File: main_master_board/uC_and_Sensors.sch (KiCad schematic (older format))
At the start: 41 parts, among them P14 CONN_01X05, U1 NRF24L01+, U15 DSPIC33EP512GP806-I/PT, U16 DWM1000, U29 RGB_LED, U30 RGB_LED, U31 Si1900DL, U32 Si1900DL, U9 Si1900DL

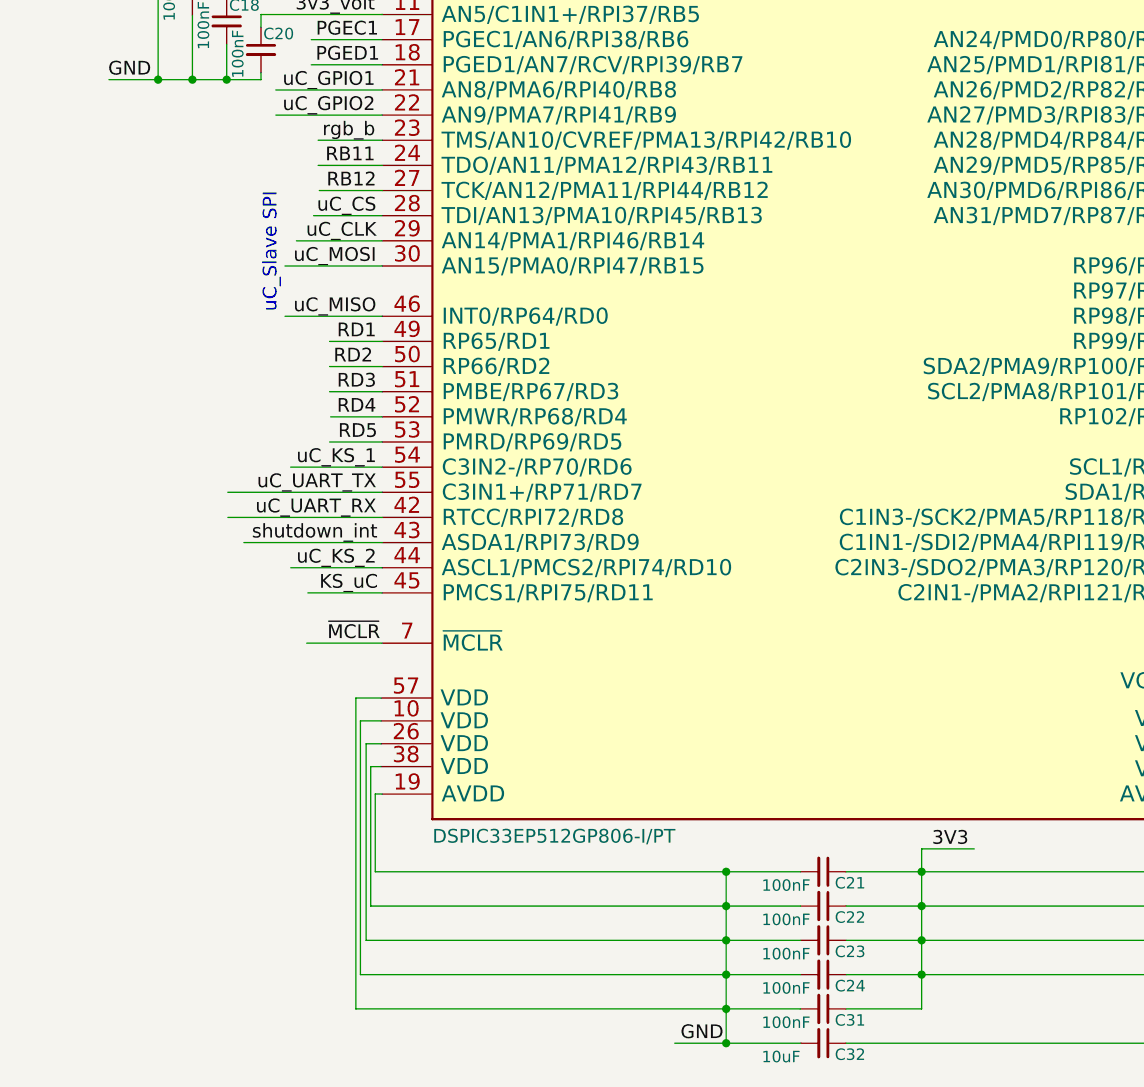
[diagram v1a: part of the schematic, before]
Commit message: more routing. Started on PIC now.
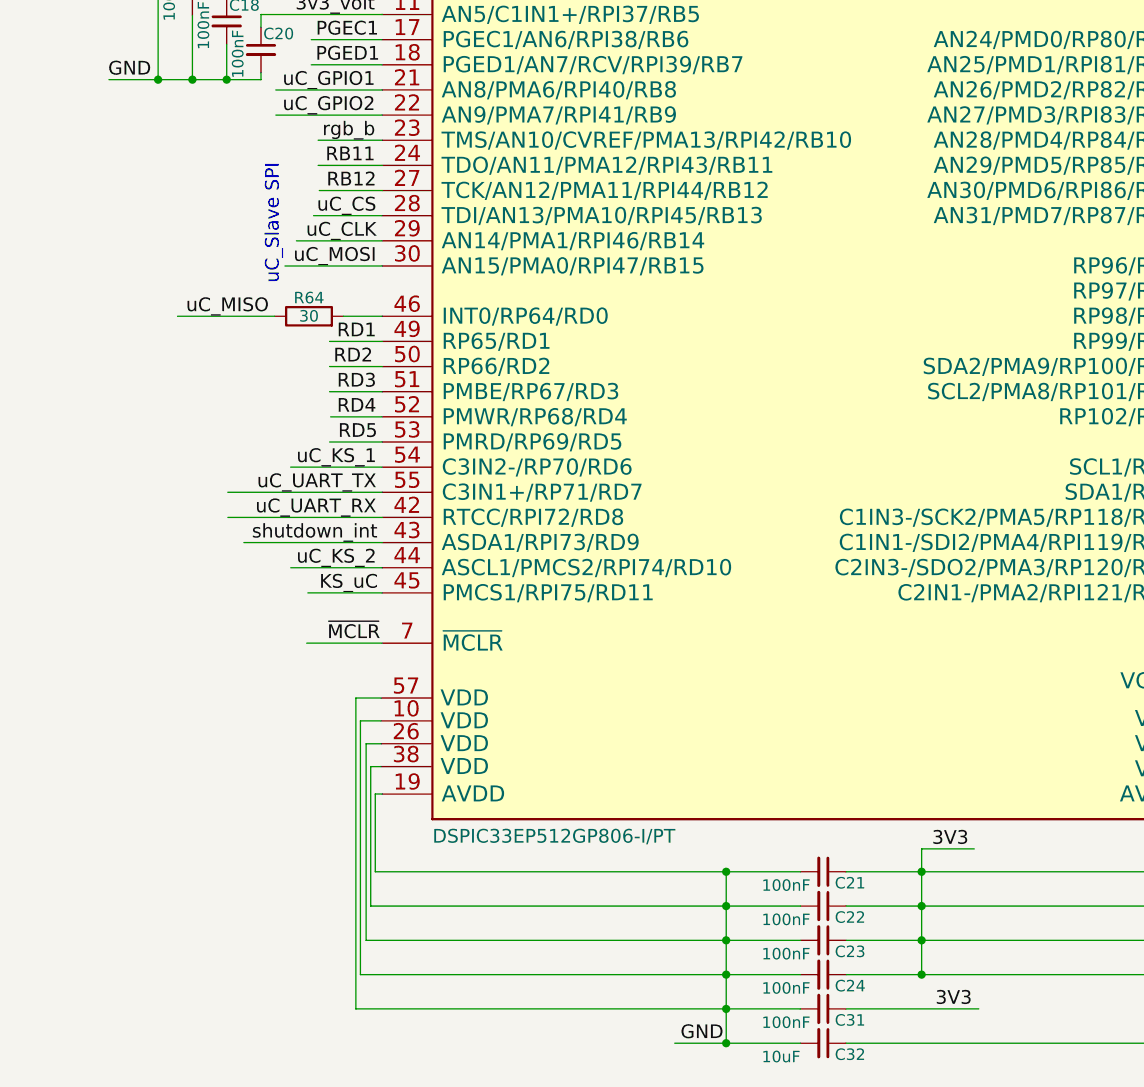
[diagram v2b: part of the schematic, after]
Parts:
- added R64: 30, Resistors_SMD:R_0402, symbol R
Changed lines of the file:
@@
 LIBS:Sensors
 LIBS:LP3852-3.3
-LIBS:decaWave
+LIBS:0s102011ma1qn1
+LIBS:74LVC1G17
+LIBS:74V1T126
+LIBS:acs711klctr-12ab-t
+LIBS:AD7192
+LIBS:AD7193
+LIBS:am-hrr30-xxx
+LIBS:aon7528
+LIBS:AP7363
+LIBS:AS1359
+LIBS:csd16323q3
+LIBS:dmn2004dmk
+LIBS:dp_devices
+LIBS:DSPIC33E128MC506
+LIBS:fds6898az
+LIBS:ina197
+LIBS:irf7329pbf
+LIBS:ld1117
+LIBS:lm3478
+LIBS:lm3481
+LIBS:lt1910
+LIBS:ltc1871
+LIBS:ltc1982
+LIBS:MAG3110
+LIBS:mcp1700
+LIBS:mcp73831
+LIBS:mcsmt-g5030a1-3712
+LIBS:microchip_can
+LIBS:microclasp_hdrx2
+LIBS:microclasp_hdrx3
+LIBS:MPU-6000_MPU-6050
+LIBS:MPU-9150
+LIBS:nrf24l01+
+LIBS:pds1040l
+LIBS:pic12f1571
+LIBS:pinhead
+LIBS:psmn013-80ys
+LIBS:RESISTOR_ARRAY
+LIBS:rf803d
+LIBS:RGB_LED
+LIBS:Si1970DH
+LIBS:sn65hvd232
+LIBS:ssc54
+LIBS:sw_push_4
+LIBS:tc74
+LIBS:TPS2113A
+LIBS:tps54540
+LIBS:vs-mbrb1635pbf
+LIBS:xal5050-562meb
+LIBS:xal6030-182mec
 LIBS:conn_2x50
 LIBS:conn_open_q_x2
@@
 LIBS:ac-dc
 LIBS:actel
-LIBS:allegro
 LIBS:Altera
 LIBS:analog_devices
@@
 LIBS:logo
 LIBS:maxim
-LIBS:mechanical
 LIBS:microchip_dspic33dsc
 LIBS:microchip_pic10mcu
@@
 LIBS:microchip_pic32mcu
 LIBS:motor_drivers
-LIBS:motors
 LIBS:msp430
 LIBS:nordicsemi
@@
 LIBS:ttl_ieee
 LIBS:video
-LIBS:wiznet
 LIBS:Worldsemi
 LIBS:Xicor
-LIBS:zetex
 LIBS:Zilog
 LIBS:conn_2x45
@@
 Text Label 9105 5345 2    60   ~ 0
 uC_MOSI
-Text Label 9105 5565 2    60   ~ 0
+Text Label 8635 5565 2    60   ~ 0
 uC_MISO
 Text Label 9105 5125 2    60   ~ 0
@@
 Text Notes 1025 2650 0    60   ~ 0
 uC_Slave SPI
-Text Notes 8675 5025 3    60   ~ 0
+Text Notes 8685 4900 3    60   ~ 0
 uC_Slave SPI
 Text Label 12895 3695 0    60   ~ 0
@@
 	9015 8595 10960 8595
 Wire Wire Line
-	11160 8595 11490 8595
-Wire Wire Line
-	11490 8595 11490 8445
-Connection ~ 11490 8445
-Wire Wire Line
-	11490 7895 11490 8440
-Connection ~ 11490 8295
-Connection ~ 11490 8145
-Connection ~ 11490 7995
+	11160 8595 11740 8595
 Wire Wire Line
 	11490 7895 11720 7895
@@
 	9130 5345 8705 5345
 Wire Wire Line
-	9130 5565 8705 5565
+	8660 5565 8235 5565
 Wire Wire Line
 	9130 5125 8830 5125
@@
 Wire Wire Line
 	9975 2625 10025 2625
+Text Label 11550 8595 0    60   ~ 0
+3V3
+Connection ~ 11490 8445
+Wire Wire Line
+	11490 7895 11490 8445
+Connection ~ 11490 8295
+Connection ~ 11490 8145
+Connection ~ 11490 7995
+$Comp
+L R R64
+U 1 1 58A3588B
+P 8810 5565
+F 0 "R64" V 8890 5565 50  0000 C CNN
+F 1 "30" V 8810 5565 50  0000 C CNN
+F 2 "Resistors_SMD:R_0402" V 8740 5565 50  0001 C CNN
+F 3 "" H 8810 5565 50  0000 C CNN
+	1    8810 5565
+	0    -1   -1   0
+$EndComp
+Wire Wire Line
+	8960 5565 9130 5565
 $EndSCHEMATC

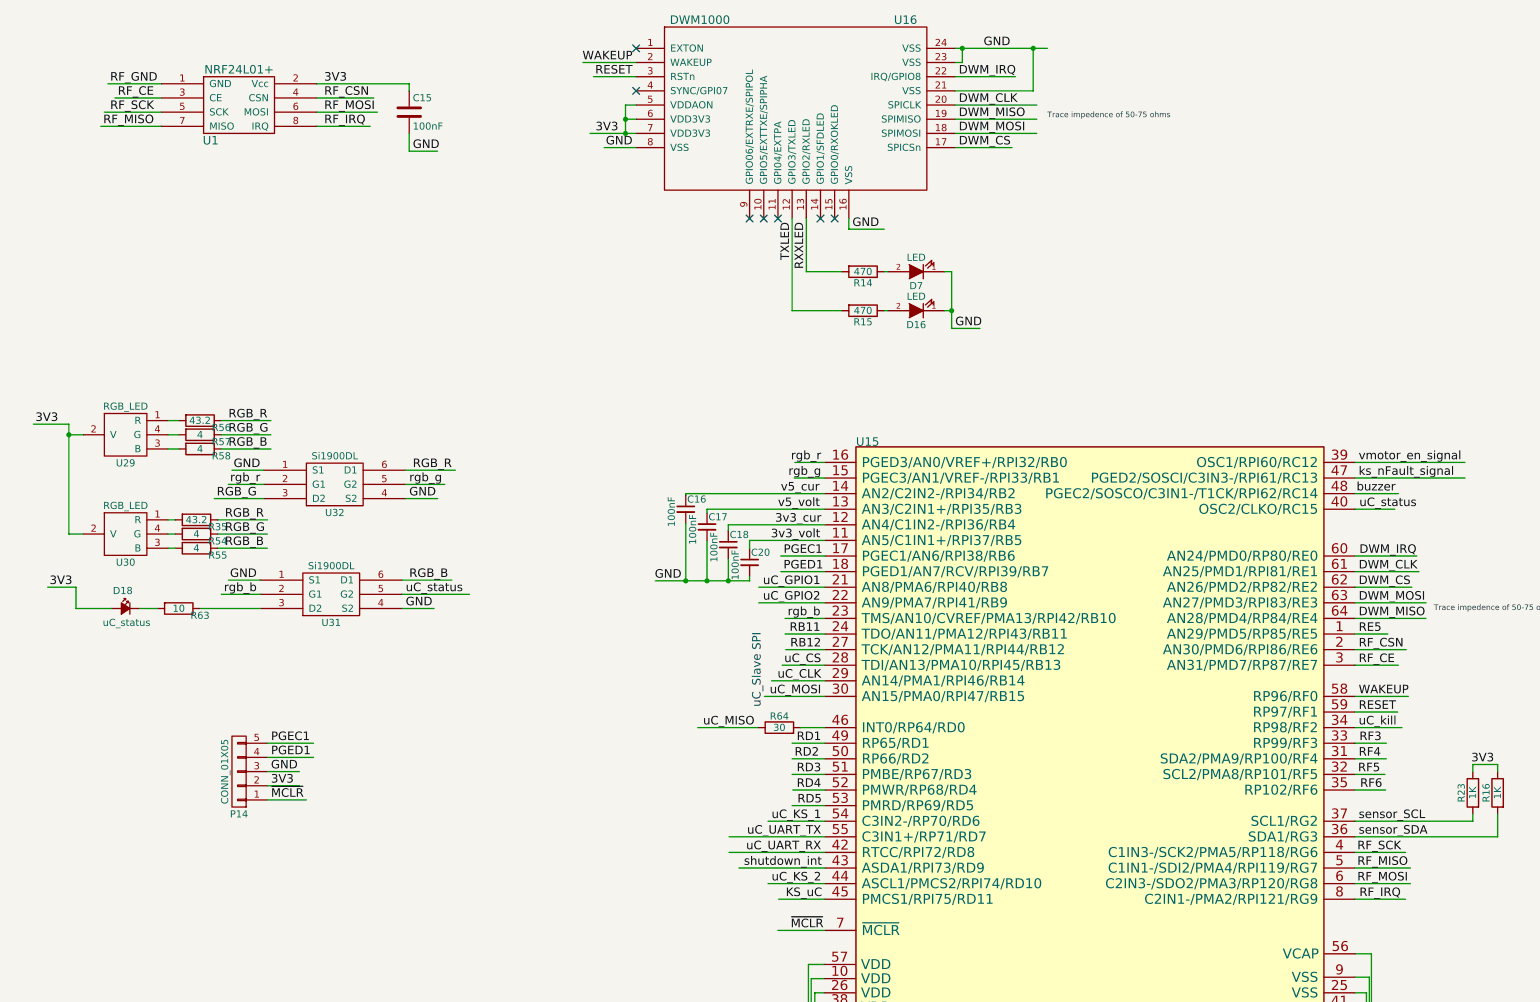
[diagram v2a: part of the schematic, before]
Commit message: Routing the RGB leds. Also finished the dwm and nrf24L01
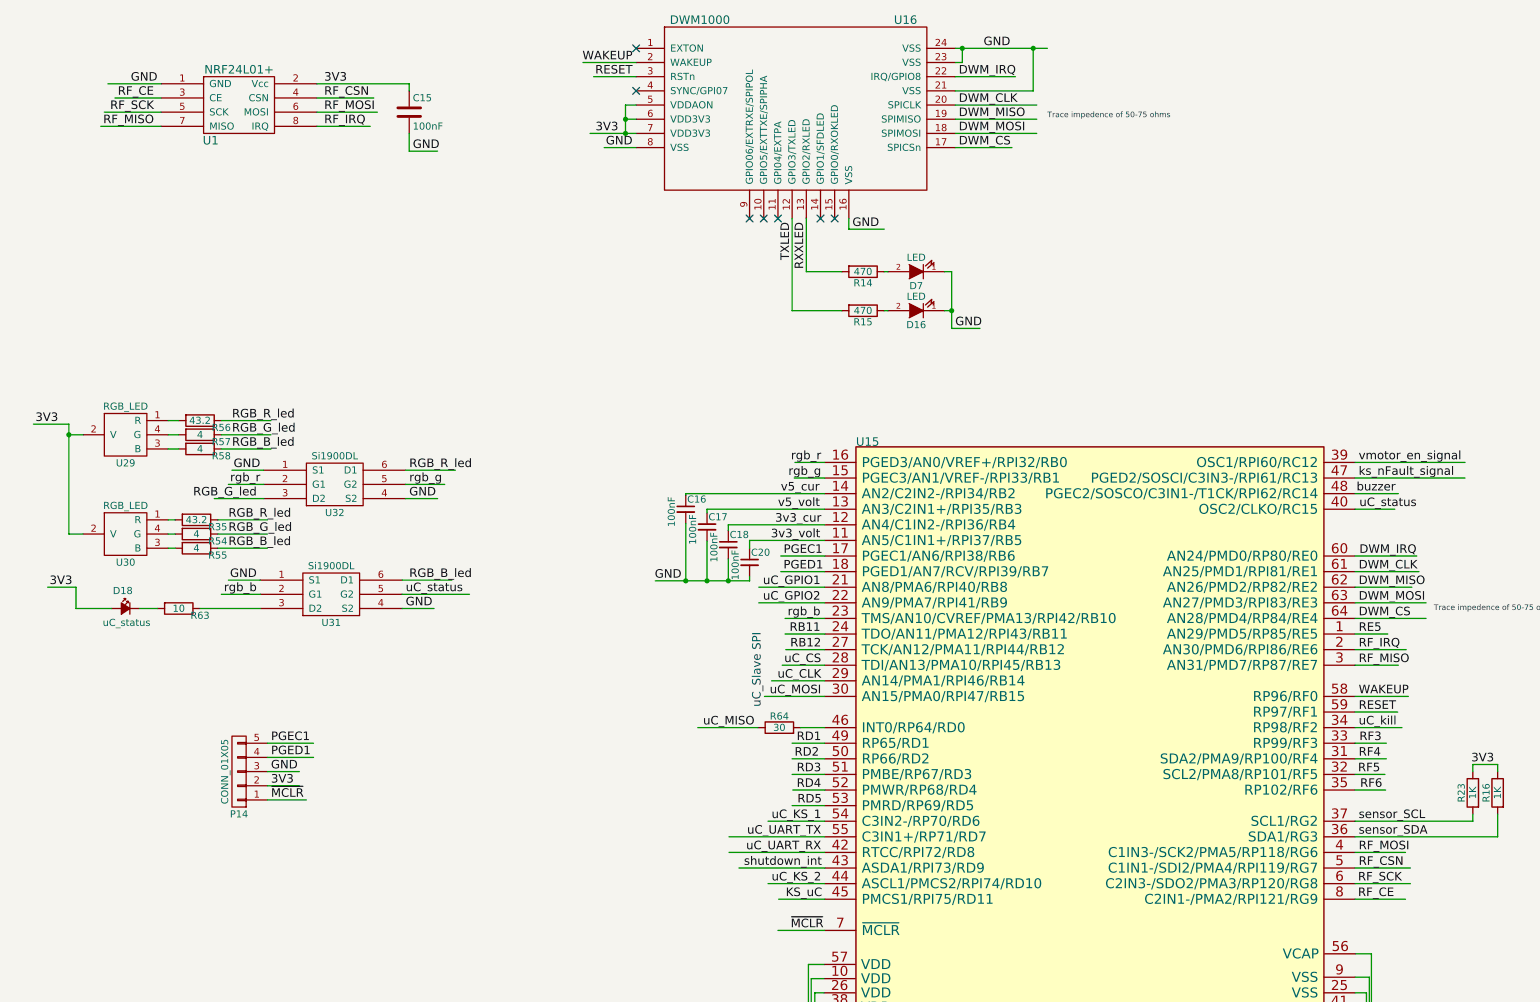
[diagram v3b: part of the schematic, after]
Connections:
- net labels added: RGB_B_led, RGB_G_led, RGB_R_led
- net labels removed: RF_GND, RGB_B, RGB_G, RGB_R
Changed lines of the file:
@@
 LIBS:Sensors
 LIBS:LP3852-3.3
-LIBS:0s102011ma1qn1
-LIBS:74LVC1G17
-LIBS:74V1T126
-LIBS:acs711klctr-12ab-t
-LIBS:AD7192
-LIBS:AD7193
-LIBS:am-hrr30-xxx
-LIBS:aon7528
-LIBS:AP7363
-LIBS:AS1359
-LIBS:csd16323q3
-LIBS:dmn2004dmk
-LIBS:dp_devices
-LIBS:DSPIC33E128MC506
-LIBS:fds6898az
-LIBS:ina197
-LIBS:irf7329pbf
-LIBS:ld1117
-LIBS:lm3478
-LIBS:lm3481
-LIBS:lt1910
-LIBS:ltc1871
-LIBS:ltc1982
-LIBS:MAG3110
-LIBS:mcp1700
-LIBS:mcp73831
-LIBS:mcsmt-g5030a1-3712
-LIBS:microchip_can
-LIBS:microclasp_hdrx2
-LIBS:microclasp_hdrx3
-LIBS:MPU-6000_MPU-6050
-LIBS:MPU-9150
-LIBS:nrf24l01+
-LIBS:pds1040l
-LIBS:pic12f1571
-LIBS:pinhead
-LIBS:psmn013-80ys
-LIBS:RESISTOR_ARRAY
-LIBS:rf803d
-LIBS:RGB_LED
-LIBS:Si1970DH
-LIBS:sn65hvd232
-LIBS:ssc54
-LIBS:sw_push_4
-LIBS:tc74
-LIBS:TPS2113A
-LIBS:tps54540
-LIBS:vs-mbrb1635pbf
-LIBS:xal5050-562meb
-LIBS:xal6030-182mec
+LIBS:decaWave
 LIBS:conn_2x50
 LIBS:conn_open_q_x2
@@
 LIBS:ac-dc
 LIBS:actel
+LIBS:allegro
 LIBS:Altera
 LIBS:analog_devices
@@
 LIBS:logo
 LIBS:maxim
+LIBS:mechanical
 LIBS:microchip_dspic33dsc
 LIBS:microchip_pic10mcu
@@
 LIBS:microchip_pic32mcu
 LIBS:motor_drivers
+LIBS:motors
 LIBS:msp430
 LIBS:nordicsemi
@@
 LIBS:ttl_ieee
 LIBS:video
+LIBS:wiznet
 LIBS:Worldsemi
 LIBS:Xicor
+LIBS:zetex
 LIBS:Zilog
 LIBS:conn_2x45
@@
 Text Label 9120 4465 2    60   ~ 0
 PGED1
-Text Label 12885 6445 0    60   ~ 0
+Text Label 12890 6665 0    60   ~ 0
 RF_SCK
-Text Label 12885 6555 0    60   ~ 0
+Text Label 12895 5125 0    60   ~ 0
 RF_MISO
-Text Label 12885 6665 0    60   ~ 0
+Text Label 12895 6445 0    60   ~ 0
 RF_MOSI
 Text Label 4425 1025 2    60   ~ 0
-RF_GND
+GND
 Text Label 4400 1125 2    60   ~ 0
 RF_CE
@@
 Text Label 6225 1500 0    60   ~ 0
 GND
-Text Label 12900 6775 0    60   ~ 0
+Text Label 12895 5015 0    60   ~ 0
 RF_IRQ
-Text Label 12895 5125 0    60   ~ 0
+Text Label 12890 6775 0    60   ~ 0
 RF_CE
 Text Label 8820 3915 0    60   ~ 0
@@
 Text Label 8750 4245 0    60   ~ 0
 3v3_volt
-Text Label 12895 5015 0    60   ~ 0
+Text Label 12895 6555 0    60   ~ 0
 RF_CSN
 $Comp
@@
 Text Label 12895 4465 0    60   ~ 0
 DWM_CLK
-Text Label 12895 4795 0    60   ~ 0
+Text Label 12895 4575 0    60   ~ 0
 DWM_MISO
 Text Label 12895 4685 0    60   ~ 0
 DWM_MOSI
-Text Label 12895 4575 0    60   ~ 0
+Text Label 12895 4795 0    60   ~ 0
 DWM_CS
 Text Label 12900 4355 0    60   ~ 0
@@
 Text Label 6200 3950 0    60   ~ 0
 GND
-Text Label 4925 3400 0    60   ~ 0
-RGB_R
-Text Label 4925 3500 0    60   ~ 0
-RGB_G
-Text Label 4925 3600 0    60   ~ 0
-RGB_B
-Text Label 4900 4100 0    60   ~ 0
-RGB_R
-Text Label 4900 4200 0    60   ~ 0
-RGB_G
-Text Label 4900 4300 0    60   ~ 0
-RGB_B
-Text Label 6225 3750 0    60   ~ 0
-RGB_R
+Text Label 4950 3400 0    60   ~ 0
+RGB_R_led
 Text Label 5125 3950 2    60   ~ 0
-RGB_G
+RGB_G_led
 $Comp
 L Si1900DL U31
@@
 GND
 Text Label 6200 4525 0    60   ~ 0
-RGB_B
+RGB_B_led
 $Comp
 L Led_Small D18
@@
 Wire Wire Line
 	8960 5565 9130 5565
+Text Label 4950 3600 0    60   ~ 0
+RGB_B_led
+Text Label 6200 3750 0    60   ~ 0
+RGB_R_led
+Text Label 4950 3500 0    60   ~ 0
+RGB_G_led
+Text Label 4925 4100 0    60   ~ 0
+RGB_R_led
+Text Label 4925 4300 0    60   ~ 0
+RGB_B_led
+Text Label 4925 4200 0    60   ~ 0
+RGB_G_led
 $EndSCHEMATC

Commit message: Added new Molex antenna. Also fixed some issues where file saves were inconsistent.
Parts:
- U1: footprint nRF2401:mini-nRF2401-SMD -> RF_Modules:nRF24L01_Breakout
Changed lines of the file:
@@
 F 0 "U1" H 4800 1325 60  0000 C CNN
 F 1 "NRF24L01+" H 5000 1825 60  0000 C CNN
-F 2 "nRF2401:mini-nRF2401-SMD" H 4750 1375 60  0001 C CNN
+F 2 "RF_Modules:nRF24L01_Breakout" H 4750 1375 60  0001 C CNN
 F 3 "" H 4750 1375 60  0000 C CNN
 F 4 "FTR-108-02-S-S" H 4750 1375 60  0001 C CNN "Field4"

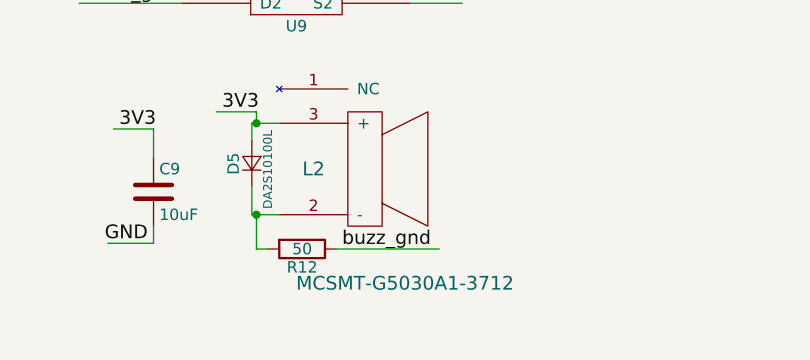
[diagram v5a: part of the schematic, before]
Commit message: Fixing minor routing issues. Also compiled BoM files for parts and positions as well as moved to different Gerber extension format for MacroFab.
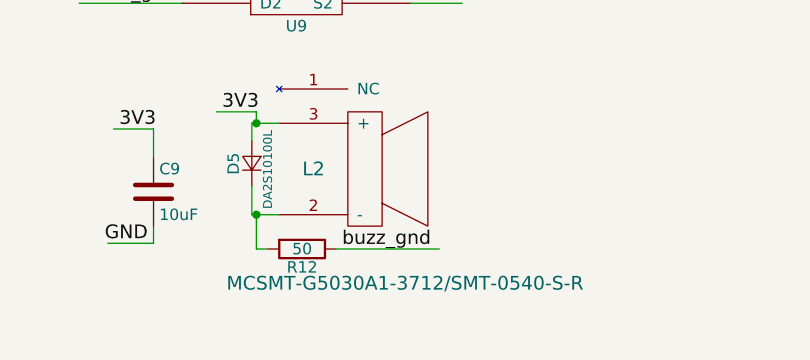
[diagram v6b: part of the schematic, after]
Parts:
- L2: value MCSMT-G5030A1-3712 -> MCSMT-G5030A1-3712/SMT-0540-S-R
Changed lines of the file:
@@
 P 1925 8400
 F 0 "L2" H 2075 8700 60  0000 C CNN
-F 1 "MCSMT-G5030A1-3712" H 2475 8200 60  0000 C CNN
+F 1 "MCSMT-G5030A1-3712/SMT-0540-S-R" H 2475 8200 60  0000 C CNN
 F 2 "MCSMT-G5030A1-3712:MCSMT-G5030A1-3712" H 1925 8400 60  0001 C CNN
 F 3 "" H 1925 8400 60  0000 C CNN

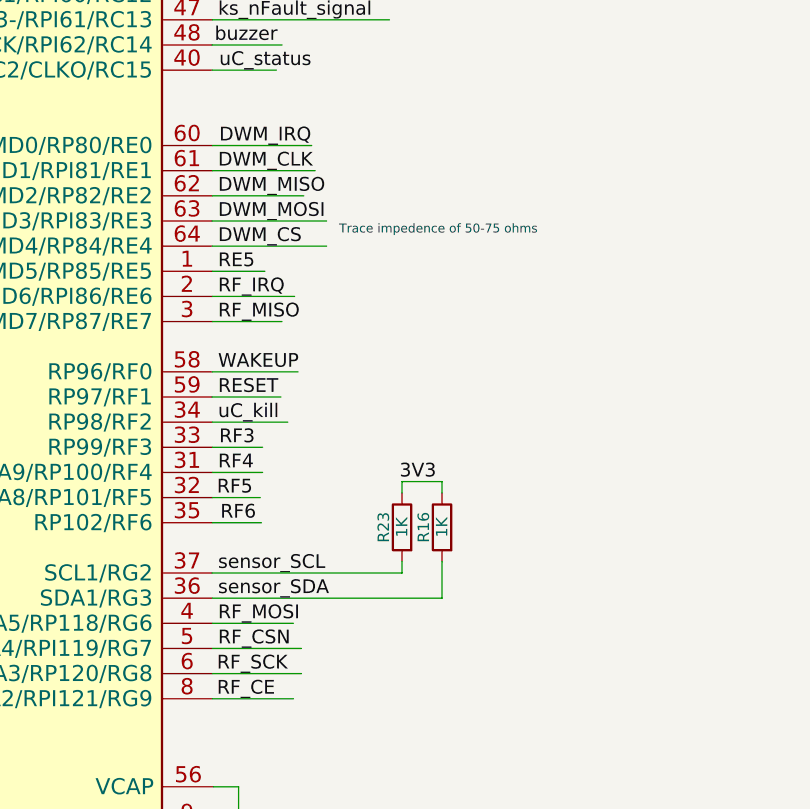
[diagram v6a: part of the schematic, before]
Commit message: Added 0ohm resistors to MISO and MOSI lines for DWM and nRF modules.
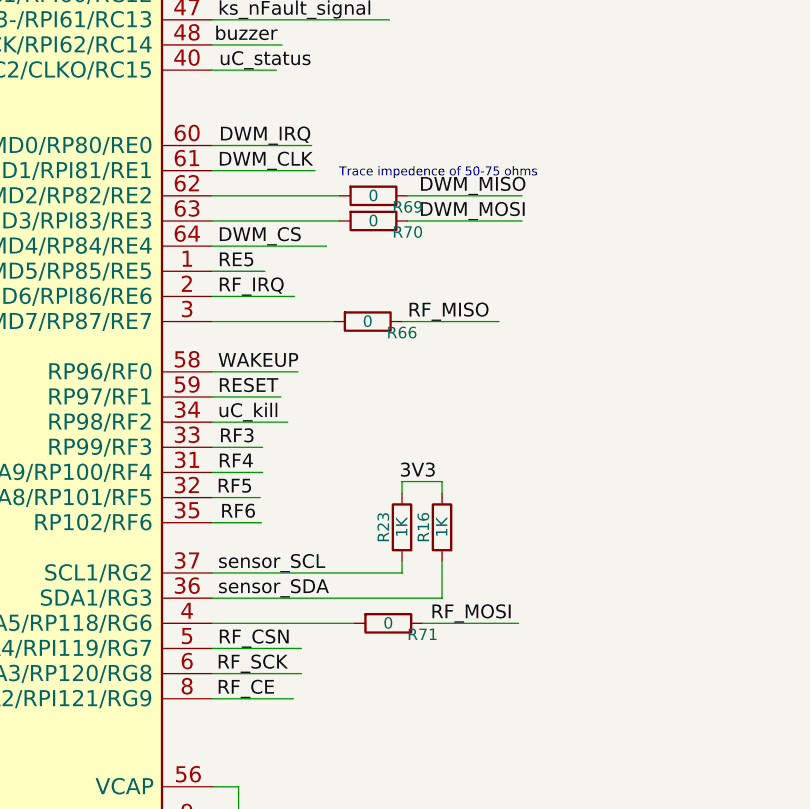
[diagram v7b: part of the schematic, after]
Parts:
- added R66, R69, R70, R71: 0, Resistors_SMD:R_0603, symbol R
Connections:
- wire segments 243 -> 247
